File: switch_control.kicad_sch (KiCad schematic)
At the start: 27 parts, among them U10 74LVC1G86, U11 74LVC1G86, U26 74HC00, U27 74LVC1G32

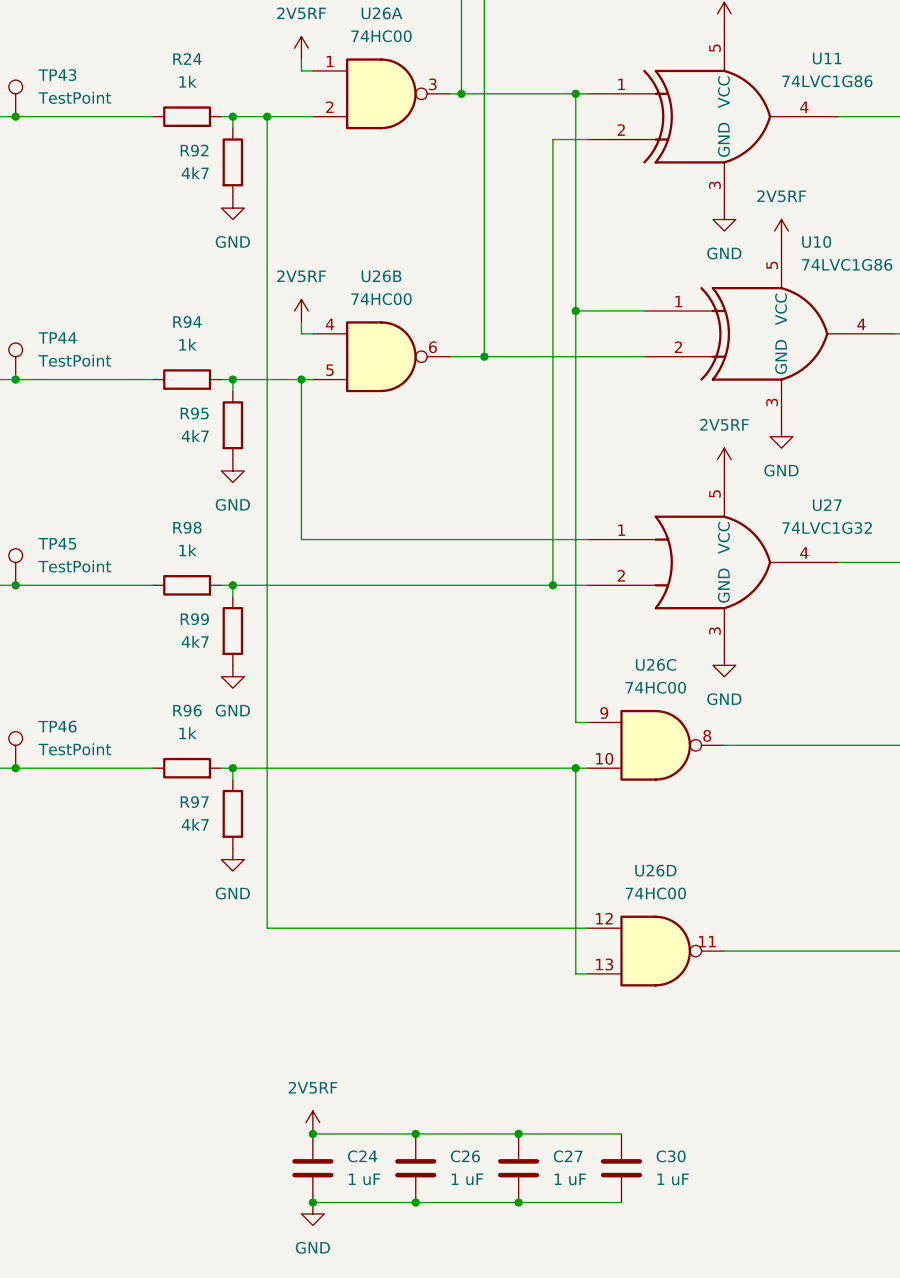
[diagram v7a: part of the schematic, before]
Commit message: Standardize component Value fields
Use Tolerance field instead of expressing tolerance in Value field
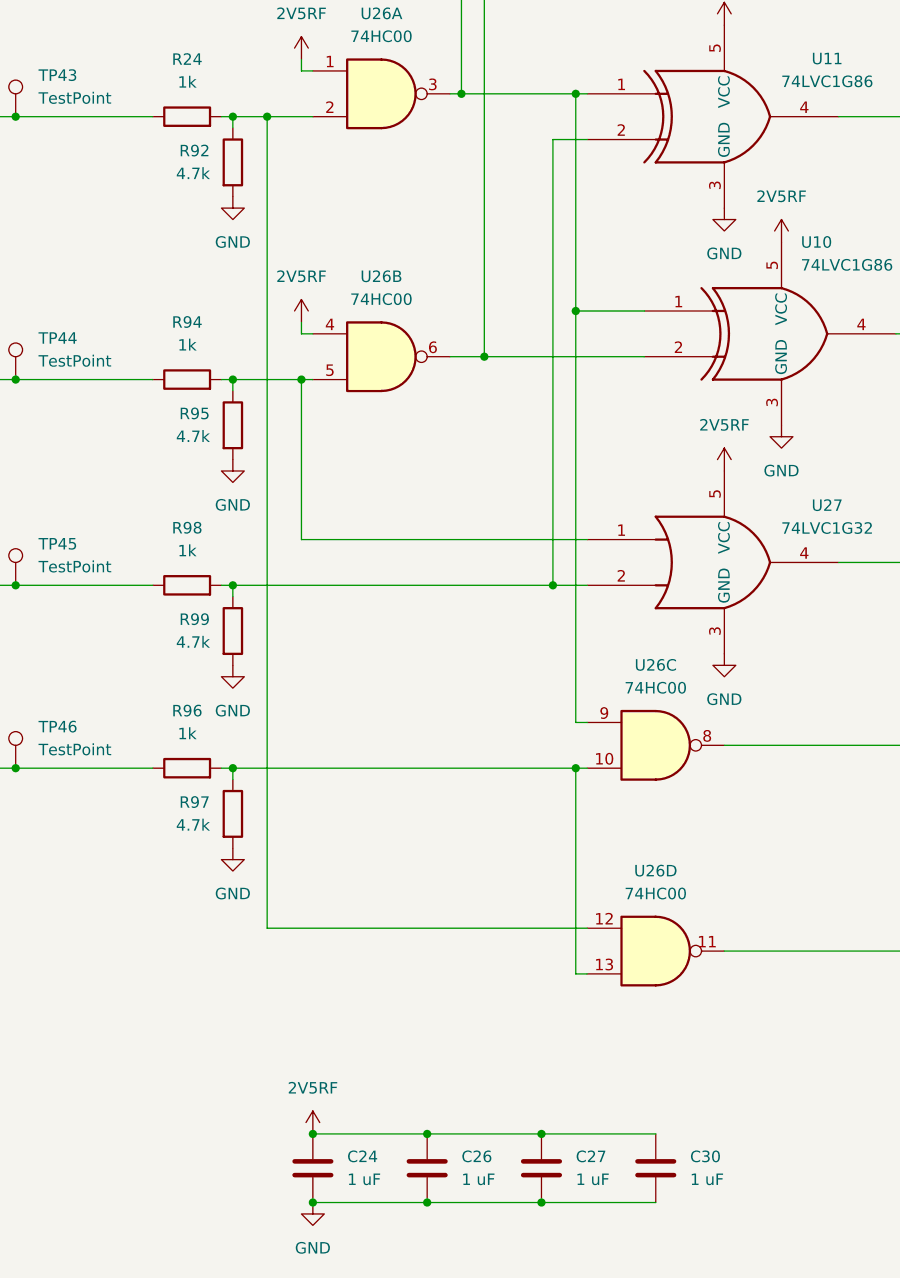
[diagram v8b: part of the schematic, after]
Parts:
- R92, R95, R97, R99: value 4k7 -> 4.7k
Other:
- moved on the sheet: C26, C27, C30
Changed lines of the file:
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@@
 	)
 	(junction
-		(at 120.65 172.72)
+		(at 121.92 172.72)
 		(diameter 0)
 		(color 0 0 0 0)
@@
 	)
 	(junction
-		(at 120.65 180.34)
+		(at 121.92 180.34)
 		(diameter 0)
 		(color 0 0 0 0)
 	)
 	(junction
-		(at 132.08 180.34)
+		(at 134.62 180.34)
 		(diameter 0)
 		(color 0 0 0 0)
@@
 	)
 	(junction
-		(at 132.08 172.72)
+		(at 134.62 172.72)
 		(diameter 0)
 		(color 0 0 0 0)
@@
 	(wire
 		(pts
-			(xy 132.08 180.34) (xy 143.51 180.34)
+			(xy 134.62 180.34) (xy 147.32 180.34)
 		)
 		(stroke
@@
 	(wire
 		(pts
-			(xy 109.22 180.34) (xy 120.65 180.34)
+			(xy 109.22 180.34) (xy 121.92 180.34)
 		)
 		(stroke
@@
 	(wire
 		(pts
-			(xy 109.22 172.72) (xy 120.65 172.72)
+			(xy 109.22 172.72) (xy 121.92 172.72)
 		)
 		(stroke
@@
 	(wire
 		(pts
-			(xy 132.08 172.72) (xy 143.51 172.72)
+			(xy 134.62 172.72) (xy 147.32 172.72)
 		)
 		(stroke
@@
 	(wire
 		(pts
-			(xy 120.65 172.72) (xy 132.08 172.72)
+			(xy 121.92 172.72) (xy 134.62 172.72)
 		)
 		(stroke
@@
 	(wire
 		(pts
-			(xy 120.65 180.34) (xy 132.08 180.34)
+			(xy 121.92 180.34) (xy 134.62 180.34)
 		)
 		(stroke
@@
 	(symbol
 		(lib_id "Device:C")
-		(at 120.65 176.53 0)
+		(at 121.92 176.53 0)
 		(unit 1)
 		(exclude_from_sim no)
@@
 		(fields_autoplaced yes)
 		(property "Reference" "C26"
-			(at 124.46 175.2599 0)
+			(at 125.73 175.2599 0)
 			(effects
 				(font
@@
 		)
 		(property "Value" "1 uF"
-			(at 124.46 177.7999 0)
+			(at 125.73 177.7999 0)
 			(effects
 				(font
@@
 		)
 		(property "Footprint" "Capacitor_SMD:C_0201_0603Metric"
-			(at 120.65 176.53 0)
+			(at 121.92 176.53 0)
 			(effects
 				(font
@@
 		)
 		(property "Datasheet" "~"
-			(at 120.65 176.53 0)
+			(at 121.92 176.53 0)
 			(effects
 				(font
@@
 		)
 		(property "Description" "CAP CER 1UF 10V X5R 0201"
-			(at 120.65 176.53 0)
+			(at 121.92 176.53 0)
 			(effects
 				(font
@@
 		)
 		(property "Manufacturer" "Murata"
-			(at 120.65 176.53 0)
+			(at 121.92 176.53 0)
 			(effects
 				(font
@@
 		)
 		(property "Part Number" "GRM033R61A105ME44D"
-			(at 120.65 176.53 0)
+			(at 121.92 176.53 0)
 			(effects
 				(font
@@
 		)
 		(property "Substitution" "GRM033R61A105ME44*, GRM033R61C105ME15*, Samsung CL03A105MO3NRN*"
-			(at 120.65 176.53 0)
+			(at 121.92 176.53 0)
 			(effects
 				(font
@@
 			)
 		)
-		(property "Value" "4k7"
+		(property "Value" "4.7k"
 			(at 97.79 138.4299 0)
 			(effects
@@
 	(symbol
 		(lib_id "Device:C")
-		(at 132.08 176.53 0)
+		(at 134.62 176.53 0)
 		(unit 1)
 		(exclude_from_sim no)
@@
 		(fields_autoplaced yes)
 		(property "Reference" "C27"
-			(at 135.89 175.2599 0)
+			(at 138.43 175.2599 0)
 			(effects
 				(font
@@
 		)
 		(property "Value" "1 uF"
-			(at 135.89 177.7999 0)
+			(at 138.43 177.7999 0)
 			(effects
 				(font
@@
 		)
 		(property "Footprint" "Capacitor_SMD:C_0201_0603Metric"
-			(at 132.08 176.53 0)
+			(at 134.62 176.53 0)
 			(effects
 				(font
@@
 		)
 		(property "Datasheet" "~"
-			(at 132.08 176.53 0)
+			(at 134.62 176.53 0)
 			(effects
 				(font
@@
 		)
 		(property "Description" "CAP CER 1UF 10V X5R 0201"
-			(at 132.08 176.53 0)
+			(at 134.62 176.53 0)
 			(effects
 				(font
@@
 		)
 		(property "Manufacturer" "Murata"
-			(at 132.08 176.53 0)
+			(at 134.62 176.53 0)
 			(effects
 				(font
@@
 		)
 		(property "Part Number" "GRM033R61A105ME44D"
-			(at 132.08 176.53 0)
+			(at 134.62 176.53 0)
 			(effects
 				(font
@@
 		)
 		(property "Substitution" "GRM033R61A105ME44*, GRM033R61C105ME15*, Samsung CL03A105MO3NRN*"
-			(at 132.08 176.53 0)
+			(at 134.62 176.53 0)
 			(effects
 				(font
@@
 			)
 		)
-		(property "Value" "4k7"
+		(property "Value" "4.7k"
 			(at 97.79 66.0399 0)
 			(effects
@@
 			)
 		)
-		(property "Value" "4k7"
+		(property "Value" "4.7k"
 			(at 97.79 118.1099 0)
 			(effects
@@
 			)
 		)
-		(property "Value" "4k7"
+		(property "Value" "4.7k"
 			(at 97.79 95.2499 0)
 			(effects
@@
 	(symbol
 		(lib_id "Device:C")
-		(at 143.51 176.53 0)
+		(at 147.32 176.53 0)
 		(unit 1)
 		(exclude_from_sim no)
@@
 		(fields_autoplaced yes)
 		(property "Reference" "C30"
-			(at 147.32 175.2599 0)
+			(at 151.13 175.2599 0)
 			(effects
 				(font
@@
 		)
 		(property "Value" "1 uF"
-			(at 147.32 177.7999 0)
+			(at 151.13 177.7999 0)
 			(effects
 				(font
@@
 		)
 		(property "Footprint" "Capacitor_SMD:C_0201_0603Metric"
-			(at 143.51 176.53 0)
+			(at 147.32 176.53 0)
 			(effects
 				(font
@@
 		)
 		(property "Datasheet" "~"
-			(at 143.51 176.53 0)
+			(at 147.32 176.53 0)
 			(effects
 				(font
@@
 		)
 		(property "Description" "CAP CER 1UF 10V X5R 0201"
-			(at 143.51 176.53 0)
+			(at 147.32 176.53 0)
 			(effects
 				(font
@@
 		)
 		(property "Manufacturer" "Murata"
-			(at 143.51 176.53 0)
+			(at 147.32 176.53 0)
 			(effects
 				(font
@@
 		)
 		(property "Part Number" "GRM033R61A105ME44D"
-			(at 143.51 176.53 0)
+			(at 147.32 176.53 0)
 			(effects
 				(font
@@
 		)
 		(property "Substitution" "GRM033R61A105ME44*, GRM033R61C105ME15*, Samsung CL03A105MO3NRN*"
-			(at 143.51 176.53 0)
+			(at 147.32 176.53 0)
 			(effects
 				(font
